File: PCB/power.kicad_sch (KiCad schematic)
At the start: 4 parts, among them J1 USB_C_Receptacle_USB2.0_16P, U2 NCP1117-3.3_TO252

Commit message: Routing PCB
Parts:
- C1, C2: footprint (none) -> Capacitor_SMD:C_0603_1608Metric_Pad1.08x0.95mm_HandSolder
- J1: footprint (none) -> Connector_USB:USB_C_Plug_Molex_105444
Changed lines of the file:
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@@
 			)
 		)
-		(property "Footprint" ""
+		(property "Footprint" "Capacitor_SMD:C_0603_1608Metric_Pad1.08x0.95mm_HandSolder"
 			(at 100.33 48.26 0)
 			(effects
@@
 			)
 		)
-		(property "Footprint" ""
+		(property "Footprint" "Capacitor_SMD:C_0603_1608Metric_Pad1.08x0.95mm_HandSolder"
 			(at 133.35 48.26 0)
 			(effects
@@
 			)
 		)
-		(property "Footprint" ""
+		(property "Footprint" "Connector_USB:USB_C_Plug_Molex_105444"
 			(at 46.99 76.2 0)
 			(effects

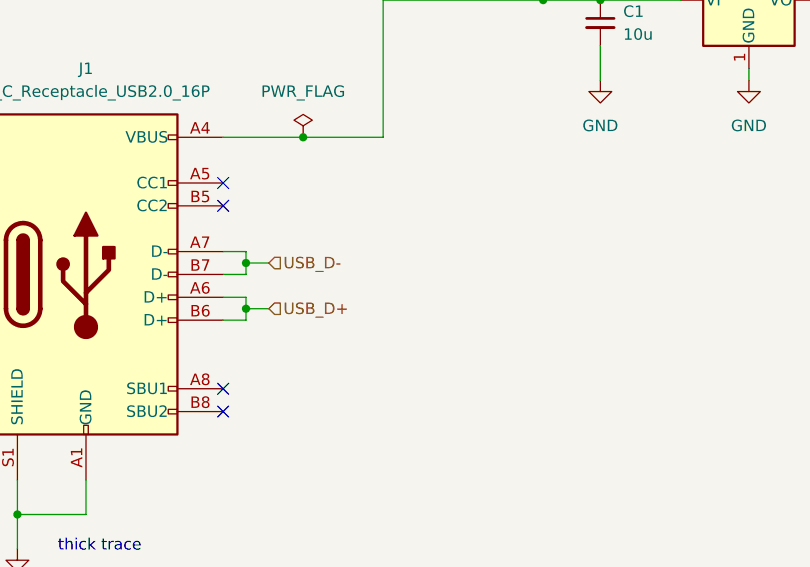
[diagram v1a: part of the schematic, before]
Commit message: Finished PCB routing
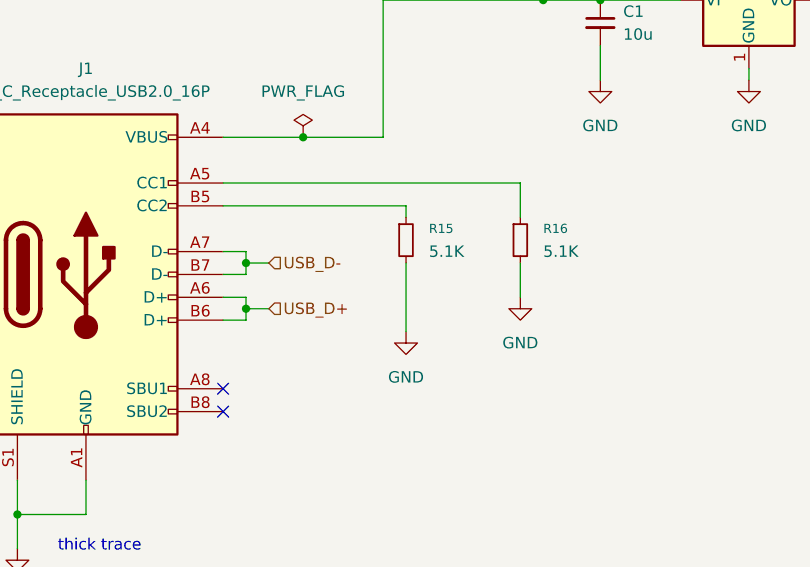
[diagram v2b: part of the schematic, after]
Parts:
- added R15, R16: 5.1K, Resistor_SMD:R_0603_1608Metric_Pad0.98x0.95mm_HandSolder, symbol Device:R_Small
- J1: footprint Connector_USB:USB_C_Plug_Molex_105444 -> Connector_USB:USB_C_Receptacle_GCT_USB4105-xx-A_16P_TopMnt_Horizontal
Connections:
- net GND: now also R15.2, R16.2
- net at J1.A5 (CC1): now also R16.1
- net at J1.B5 (CC2): now also R15.1
- no-connect marks 4 -> 2

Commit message: Writeup + case
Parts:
- added D4, D5: 1N5819WS, Diode_SMD:D_SOD-323, symbol Diode:1N5819WS
- added J12: Conn_01x02_Pin, Connector_PinHeader_2.54mm:PinHeader_1x02_P2.54mm_Vertical, symbol Connector:Conn_01x02_Pin
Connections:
- net GND: now also J12.2 (Pin_2)
- net VBUS: now also D4.1 (K), D5.1 (K); no longer J1.A4 (VBUS), J1.A9 (VBUS), J1.B4 (VBUS), J1.B9 (VBUS)
- new net: D5.2 (A), J12.1 (Pin_1)
- new net: D4.2 (A), J1.A4 (VBUS), J1.A9 (VBUS), J1.B4 (VBUS), J1.B9 (VBUS)
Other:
- moved on the sheet: C1, C2, U2

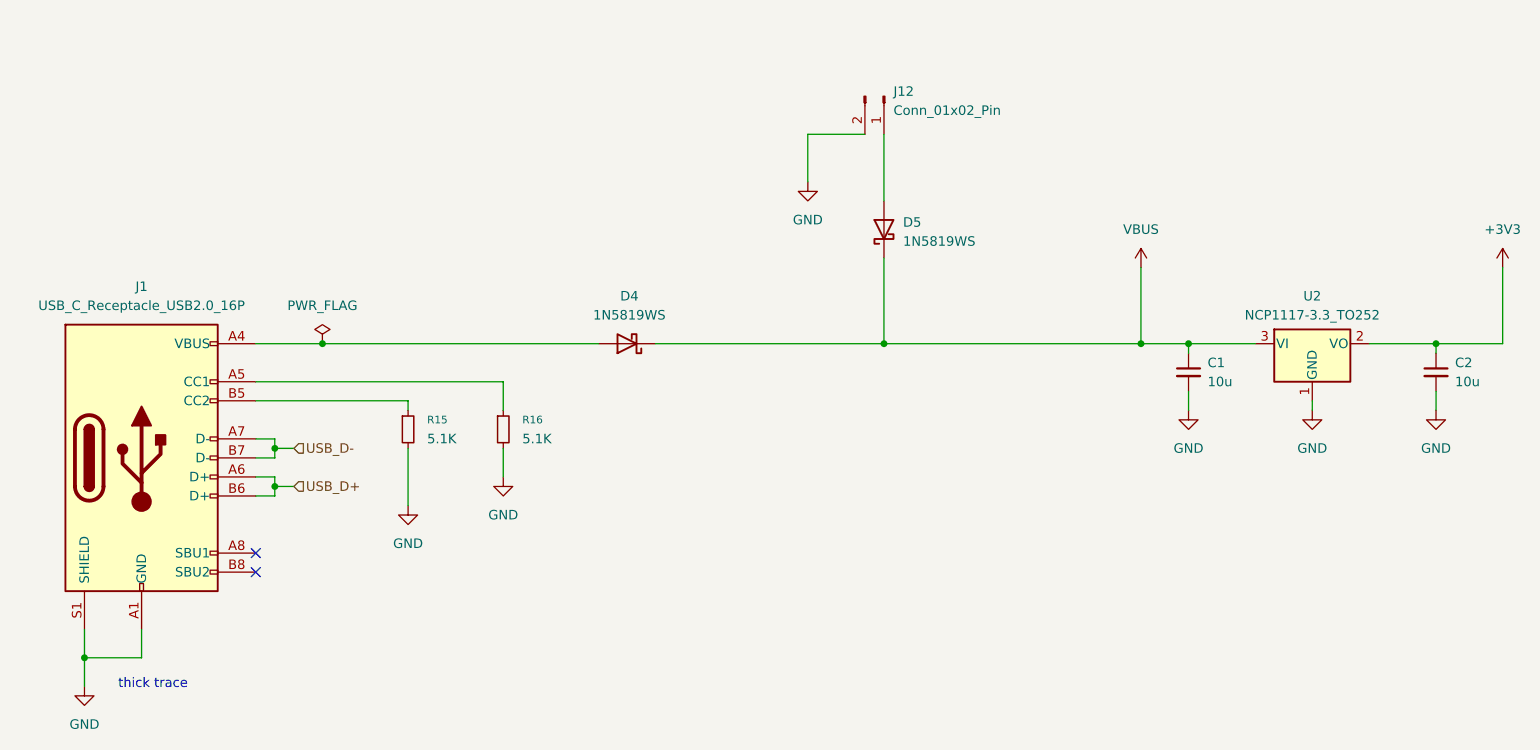
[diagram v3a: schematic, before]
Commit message: esd, pullup, error fix
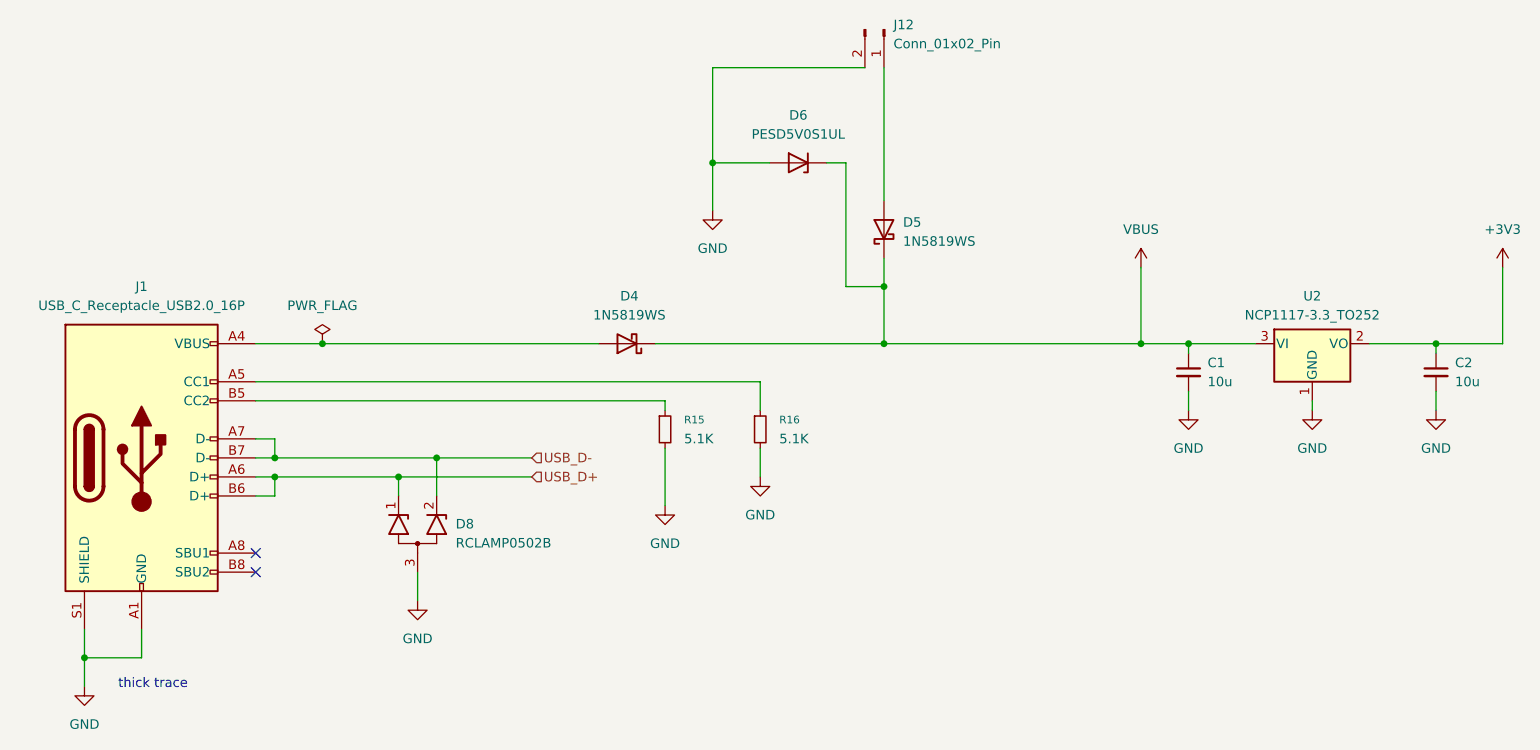
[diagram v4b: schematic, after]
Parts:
- added D6: PESD5V0S1UL, Diode_SMD:D_SOD-882, symbol Diode:PESD5V0S1UL
- added D8: RCLAMP0502B, Package_TO_SOT_SMD:SOT-416, symbol Power_Protection:RCLAMP0502B
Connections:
- net GND: now also D6.2 (A), D8.3 (A)
- net USB_D+: now also D8.1 (K1)
- net USB_D-: now also D8.2 (K2)
- net VBUS: now also D6.1 (K)
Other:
- moved on the sheet: J12, R15, R16
